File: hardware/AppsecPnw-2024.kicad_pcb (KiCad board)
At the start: 2 copper layers, 75.2 x 76.5 mm, 45 parts, among them J1 OLED, J2 Battery, J3 Conn_02x03_Odd_Even, J5 UART, P1 USB_C_Plug_USB2.0, Q1 DMG3415U-7, SW1 ON, SW2 LEFT, SW3 DOWN, SW4 UP, SW5 RIGTH, SW6 RESET, SW7 BOOT, U2 ESP32-C6-WROOM-1-N4, U4 AP2112K-3.3

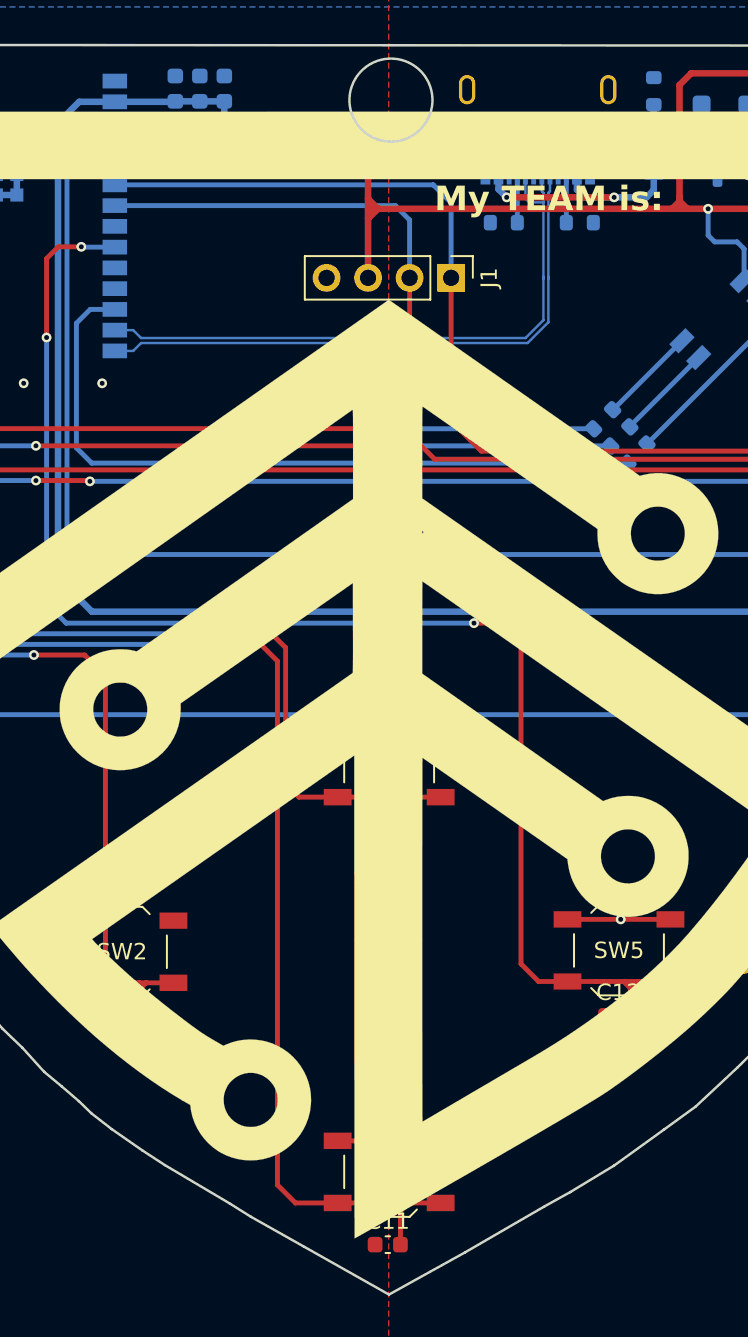
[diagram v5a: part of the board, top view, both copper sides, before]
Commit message: feat(Hw): Update labels
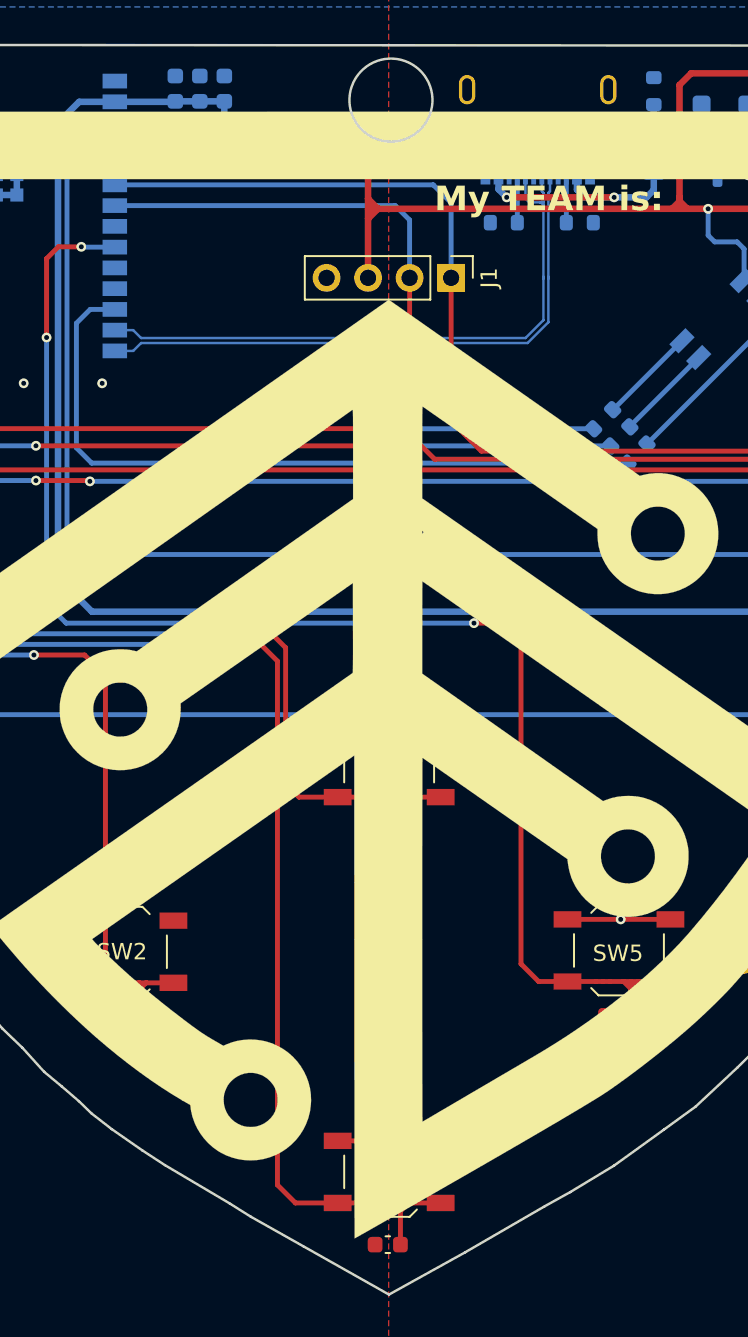
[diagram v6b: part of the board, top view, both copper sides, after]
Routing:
- net /D-: track 38.9 -> 39.4 mm

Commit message: feat(hw): lables rst and boot
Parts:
- added kibuzzard-6616FF4C: G***, kibuzzard-6616FF4C, B.Cu at (230.1, 58.4)
- added kibuzzard-6616FF56: G***, kibuzzard-6616FF56, B.Cu at (228.2, 70.0)

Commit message: feat(hw): add labels on/off
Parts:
- added kibuzzard-66170030: G***, kibuzzard-66170030, B.Cu at (233.2, 47.5)
- added kibuzzard-6617003A: G***, kibuzzard-6617003A, B.Cu at (233.3, 38.6)
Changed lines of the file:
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@@
+		)
+	)
+	(footprint "kibuzzard-6617003A"
+		(layer "B.Cu")
+		(at 233.35 38.61 180)
+		(descr "Generated with KiBuzzard")
+		(tags "kb_params=eyJBbGlnbm1lbnRDaG9pY2UiOiAiQ2VudGVyIiwgIkNhcExlZnRDaG9pY2UiOiAiWyIsICJDYXBSaWdodENob2ljZSI6ICJdIiwgIkZvbnRDb21ib0JveCI6ICJVYnVudHVNb25vLUIiLCAiSGVpZ2h0Q3RybCI6ICIxIiwgIkxheWVyQ29tYm9Cb3giOiAiRi5TaWxrUyIsICJNdWx0aUxpbmVUZXh0IjogIk9GRiIsICJQYWRkaW5nQm90dG9tQ3RybCI6ICI1IiwgIlBhZGRpbmdMZWZ0Q3RybCI6ICI1IiwgIlBhZGRpbmdSaWdodEN0cmwiOiAiNSIsICJQYWRkaW5nVG9wQ3RybCI6ICI1IiwgIldpZHRoQ3RybCI6ICIifQ==")
+		(property "Reference" "kibuzzard-6617003A"
+			(at 0 3.891492 180)
+			(layer "B.SilkS")
+			(hide yes)
+			(effects
+				(font
+					(size 0.0254 0.0254)
+				)
+				(justify mirror)
+			)
+		)
+		(property "Value" "G***"
+			(at 0 -3.891492 180)
+			(layer "B.SilkS")
+			(hide yes)
+			(effects
+				(font
+					(size 0.0254 0.0254)
+				)
+				(justify mirror)
+			)
+		)
+		(property "Footprint" ""
+			(at 0 0 0)
+			(unlocked yes)
+			(layer "B.Fab")
+			(hide yes)
+			(effects
+				(font
+					(size 1.27 1.27)
+				)
+				(justify mirror)
+			)
+		)
+		(property "Datasheet" ""
+			(at 0 0 0)
+			(unlocked yes)
+			(layer "B.Fab")
+			(hide yes)
+			(effects
+				(font
+					(size 1.27 1.27)
+				)
+				(justify mirror)
+			)
+		)
+		(property "Description" ""
+			(at 0 0 0)
+			(unlocked yes)
+			(layer "B.Fab")
+			(hide yes)
+			(effects
+				(font
+					(size 1.27 1.27)
+				)
+				(justify mirror)
+			)
+		)
+		(attr board_only exclude_from_pos_files exclude_from_bom)
+		(fp_poly
+			(pts
+				(xy -0.924719 0) (xy -0.92333 -0.069255) (xy -0.919163 -0.134144) (xy -0.896938 -0.242887) (xy -0.850106 -0.315912)
+				(xy -0.769144 -0.3429) (xy -0.688975 -0.315912) (xy -0.64135 -0.242094) (xy -0.619125 -0.13335)
+				(xy -0.614958 -0.069056) (xy -0.613569 0) (xy -0.614958 0.069255) (xy -0.619125 0.134144) (xy -0.64135 0.242888)
+				(xy -0.688181 0.315913) (xy -0.769144 0.3429) (xy -0.850106 0.315913) (xy -0.896938 0.242094) (xy -0.919163 0.13335)
+				(xy -0.92333 0.069056) (xy -0.924719 0)
+			)
+			(stroke
+				(width 0)
+				(type solid)
+			)
+			(fill solid)
+			(layer "B.SilkS")
+		)
+		(fp_poly
+			(pts
+				(xy -1.123156 0.843492) (xy -1.453885 0.843492) (xy -1.453885 -0.843492) (xy -1.123156 -0.843492)
+				(xy -0.767556 -0.843492) (xy -0.767556 -0.512762) (xy -0.873831 -0.498387) (xy -0.961937 -0.45526)
+				(xy -1.031875 -0.383381) (xy -1.071811 -0.310902) (xy -1.100336 -0.222845) (xy -1.117451 -0.119211)
+				(xy -1.123156 0) (xy -1.117302 0.119211) (xy -1.099741 0.222845) (xy -1.070471 0.310902) (xy -1.029494 0.383381)
+				(xy -0.958938 0.45526) (xy -0.872155 0.498387) (xy -0.769144 0.512763) (xy -0.662958 0.498387) (xy -0.575116 0.45526)
+				(xy -0.505619 0.383381) (xy -0.46603 0.310902) (xy -0.437753 0.222845) (xy -0.420787 0.119211) (xy -0.415131 0)
+				(xy -0.420886 -0.119211) (xy -0.43815 -0.222845) (xy -0.466923 -0.310902) (xy -0.507206 -0.383381)
+				(xy -0.577056 -0.45526) (xy -0.66384 -0.498387) (xy -0.767556 -0.512762) (xy -0.767556 -0.843492)
+				(xy -0.272256 -0.843492) (xy -0.272256 -0.492125) (xy -0.272256 0.490538) (xy 0.329406 0.490538)
+				(xy 0.329406 0.328613) (xy -0.076994 0.328613) (xy -0.076994 0.090488) (xy 0.278606 0.090488) (xy 0.278606 -0.071437)
+				(xy -0.076994 -0.071437) (xy -0.076994 -0.492125) (xy -0.272256 -0.492125) (xy -0.272256 -0.843492)
+				(xy 0.521494 -0.843492) (xy 0.521494 -0.492125) (xy 0.521494 0.490538) (xy 1.123156 0.490538) (xy 1.123156 0.328613)
+				(xy 0.716756 0.328613) (xy 0.716756 0.090488) (xy 1.072356 0.090488) (xy 1.072356 -0.071437) (xy 0.716756 -0.071437)
+				(xy 0.716756 -0.492125) (xy 0.521494 -0.492125) (xy 0.521494 -0.843492) (xy 1.123156 -0.843492)
+				(xy 1.453885 -0.843492) (xy 1.453885 0.843492) (xy 1.123156 0.843492) (xy -1.123156 0.843492)
+			)
+			(stroke
+				(width 0)
+				(type solid)
+			)
+			(fill solid)
+			(layer "B.SilkS")
 		)
 	)
@@
 			)
 			(stroke
+				(width 0)
+				(type solid)
+			)
+			(fill solid)
+			(layer "B.SilkS")
+		)
+	)
+	(footprint "kibuzzard-66170030"
+		(layer "B.Cu")
+		(at 233.24 47.54 180)
+		(descr "Generated with KiBuzzard")
+		(tags "kb_params=eyJBbGlnbm1lbnRDaG9pY2UiOiAiQ2VudGVyIiwgIkNhcExlZnRDaG9pY2UiOiAiWyIsICJDYXBSaWdodENob2ljZSI6ICJdIiwgIkZvbnRDb21ib0JveCI6ICJVYnVudHVNb25vLUIiLCAiSGVpZ2h0Q3RybCI6ICIxIiwgIkxheWVyQ29tYm9Cb3giOiAiRi5TaWxrUyIsICJNdWx0aUxpbmVUZXh0IjogIk9OIiwgIlBhZGRpbmdCb3R0b21DdHJsIjogIjUiLCAiUGFkZGluZ0xlZnRDdHJsIjogIjUiLCAiUGFkZGluZ1JpZ2h0Q3RybCI6ICI1IiwgIlBhZGRpbmdUb3BDdHJsIjogIjUiLCAiV2lkdGhDdHJsIjogIiJ9")
+		(property "Reference" "kibuzzard-66170030"
+			(at 0 3.891492 180)
+			(layer "B.SilkS")
+			(hide yes)
+			(effects
+				(font
+					(size 0.0254 0.0254)
+				)
+				(justify mirror)
+			)
+		)
+		(property "Value" "G***"
+			(at 0 -3.891492 180)
+			(layer "B.SilkS")
+			(hide yes)
+			(effects
+				(font
+					(size 0.0254 0.0254)
+				)
+				(justify mirror)
+			)
+		)
+		(property "Footprint" ""
+			(at 0 0 0)
+			(unlocked yes)
+			(layer "B.Fab")
+			(hide yes)
+			(effects
+				(font
+					(size 1.27 1.27)
+				)
+				(justify mirror)
+			)
+		)
+		(property "Datasheet" ""
+			(at 0 0 0)
+			(unlocked yes)
+			(layer "B.Fab")
+			(hide yes)
+			(effects
+				(font
+					(size 1.27 1.27)
+				)
+				(justify mirror)
+			)
+		)
+		(property "Description" ""
+			(at 0 0 0)
+			(unlocked yes)
+			(layer "B.Fab")
+			(hide yes)
+			(effects
+				(font
+					(size 1.27 1.27)
+				)
+				(justify mirror)
+			)
+		)
+		(attr board_only exclude_from_pos_files exclude_from_bom)
+		(fp_poly
+			(pts
+				(xy -0.537369 0) (xy -0.53598 -0.069255) (xy -0.531813 -0.134144) (xy -0.509588 -0.242887) (xy -0.462756 -0.315912)
+				(xy -0.381794 -0.3429) (xy -0.301625 -0.315912) (xy -0.254 -0.242094) (xy -0.231775 -0.13335) (xy -0.227608 -0.069056)
+				(xy -0.226219 0) (xy -0.227608 0.069255) (xy -0.231775 0.134144) (xy -0.254 0.242888) (xy -0.300831 0.315913)
+				(xy -0.381794 0.3429) (xy -0.462756 0.315913) (xy -0.509588 0.242094) (xy -0.531813 0.13335) (xy -0.53598 0.069056)
+				(xy -0.537369 0)
+			)
+			(stroke
+				(width 0)
+				(type solid)
+			)
+			(fill solid)
+			(layer "B.SilkS")
+		)
+		(fp_poly
+			(pts
+				(xy -0.735806 0.843492) (xy -1.066535 0.843492) (xy -1.066535 -0.843492) (xy -0.735806 -0.843492)
+				(xy -0.380206 -0.843492) (xy -0.380206 -0.512762) (xy -0.486481 -0.498387) (xy -0.574587 -0.45526)
+				(xy -0.644525 -0.383381) (xy -0.684461 -0.310902) (xy -0.712986 -0.222845) (xy -0.730101 -0.119211)
+				(xy -0.735806 0) (xy -0.729952 0.119211) (xy -0.712391 0.222845) (xy -0.683121 0.310902) (xy -0.642144 0.383381)
+				(xy -0.571588 0.45526) (xy -0.484805 0.498387) (xy -0.381794 0.512763) (xy -0.275608 0.498387) (xy -0.187766 0.45526)
+				(xy -0.118269 0.383381) (xy -0.07868 0.310902) (xy -0.050403 0.222845) (xy -0.033437 0.119211) (xy -0.027781 0)
+				(xy -0.033536 -0.119211) (xy -0.0508 -0.222845) (xy -0.079573 -0.310902) (xy -0.119856 -0.383381)
+				(xy -0.189706 -0.45526) (xy -0.27649 -0.498387) (xy -0.380206 -0.512762) (xy -0.380206 -0.843492)
+				(xy 0.578644 -0.843492) (xy 0.578644 -0.492125) (xy 0.532871 -0.383205) (xy 0.484452 -0.274461)
+				(xy 0.433387 -0.165894) (xy 0.379677 -0.057326) (xy 0.323321 0.051417) (xy 0.264319 0.160338) (xy 0.264319 -0.492125)
+				(xy 0.088106 -0.492125) (xy 0.088106 0.490538) (xy 0.245269 0.490538) (xy 0.289719 0.417711) (xy 0.334169 0.338931)
+				(xy 0.378023 0.257373) (xy 0.420688 0.176213) (xy 0.461169 0.096441) (xy 0.498475 0.01905) (xy 0.531614 -0.052387)
+				(xy 0.559594 -0.1143) (xy 0.559594 0.490538) (xy 0.735806 0.490538) (xy 0.735806 -0.492125) (xy 0.578644 -0.492125)
+				(xy 0.578644 -0.843492) (xy 0.735806 -0.843492) (xy 1.066535 -0.843492) (xy 1.066535 0.843492) (xy 0.735806 0.843492)
+				(xy -0.735806 0.843492)
+			)
+			(stroke
